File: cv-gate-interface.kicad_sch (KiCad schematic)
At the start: 19 parts, among them J3 Conn_01x06_Pin, J4 Conn_01x06_Pin, SW1 SW_SPST, U1 TL072

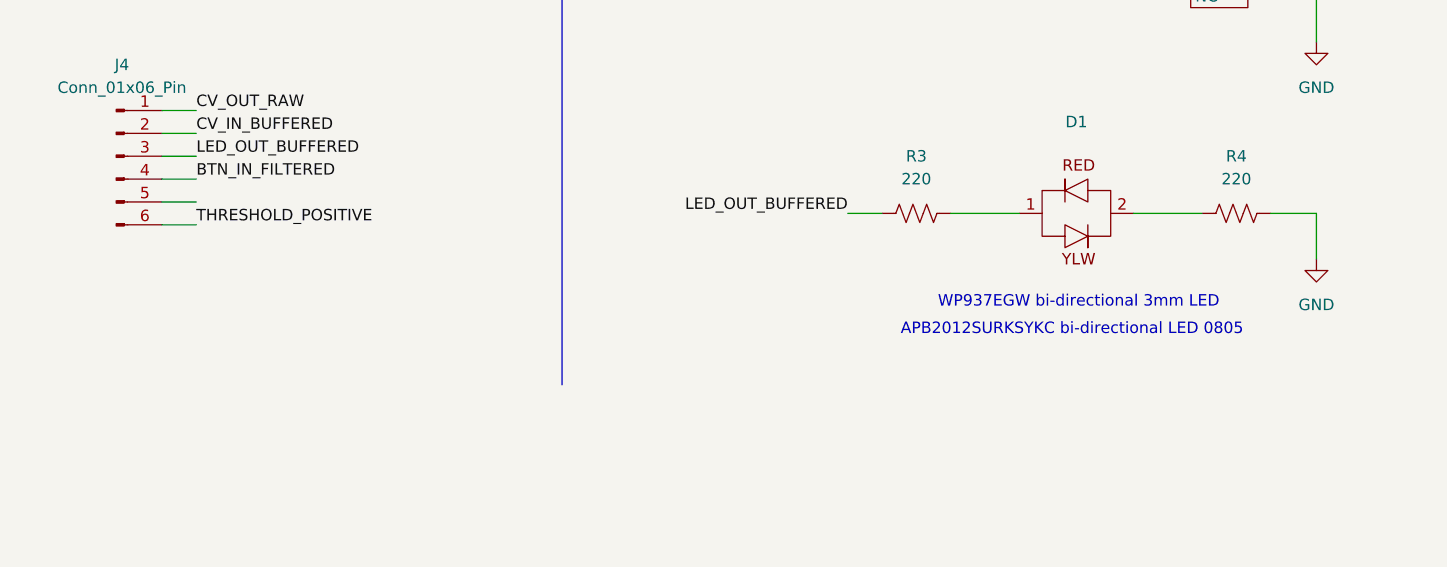
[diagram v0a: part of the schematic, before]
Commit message: Changed pot to 10K, fixed routing
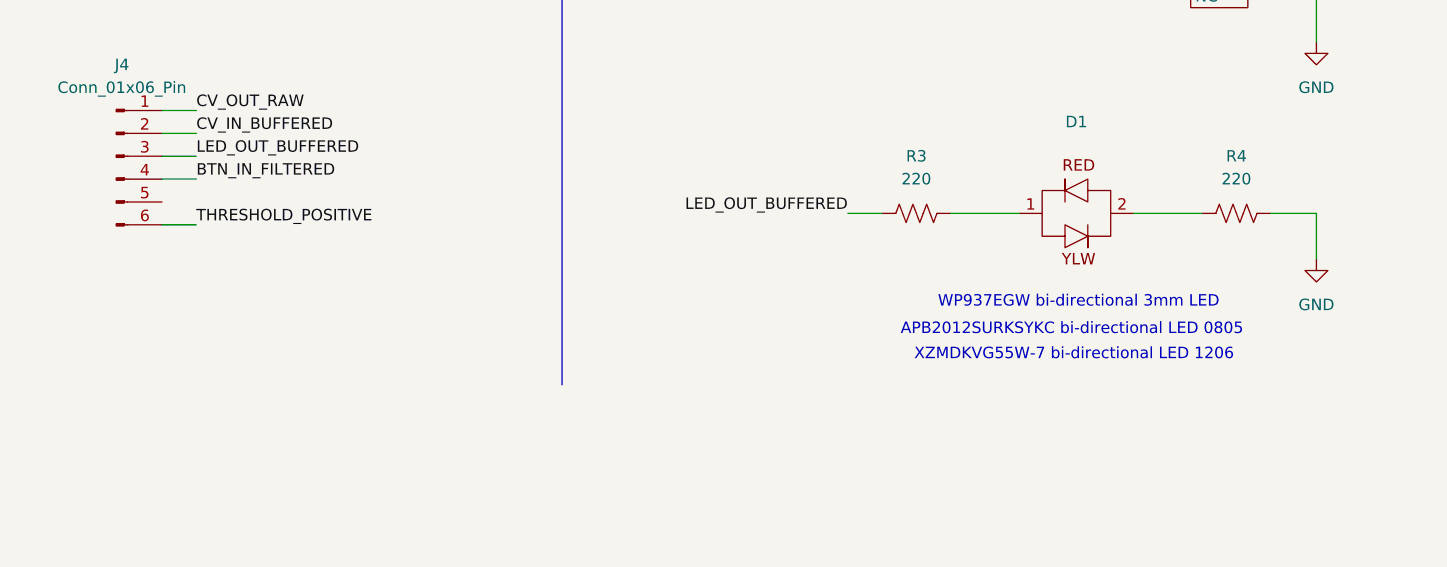
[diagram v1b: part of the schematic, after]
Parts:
- removed D1: ~, LED_THT:LED_D3.0mm, symbol mjrskiles:WP937EGW
- added D1: ~, mjrskiles:XZMDKVG55W-7, symbol mjrskiles:LED_BIPOLAR
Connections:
- net at R4.1: now also D1.2
- net at R3.2: now also D1.1
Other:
- note added: "XZMDKVG55W-7 bi-directional LED 1206"
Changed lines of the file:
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@@
+		)
+	)
+	(text "XZMDKVG55W-7 bi-directional LED 1206"
+		(exclude_from_sim no)
+		(at 234.696 160.528 0)
+		(effects
+			(font
+				(size 1.27 1.27)
+			)
 		)
 	)
@@
 		(pts
 			(xy 39.37 44.45) (xy 44.45 44.45)
-		)
-		(stroke
-			(width 0)
-			(type default)
-		)
-	)
-	(wire
-		(pts
-			(xy 133.35 143.51) (xy 137.16 143.51)
 		)
 		(stroke
@@
 	)
 	(symbol
+		(lib_id "mjrskiles:LED_BIPOLAR")
+		(at 233.68 144.78 0)
+		(unit 1)
+		(exclude_from_sim no)
+		(in_bom yes)
+		(on_board yes)
+		(dnp no)
+		(fields_autoplaced yes)
+		(property "Reference" "D1"
+			(at 234.95 134.62 0)
+			(effects
+				(font
+					(size 1.27 1.27)
+				)
+			)
+		)
+		(property "Value" "~"
+			(at 234.95 137.16 0)
+			(effects
+				(font
+					(size 1.27 1.27)
+				)
+			)
+		)
+		(property "Footprint" "mjrskiles:XZMDKVG55W-7"
+			(at 233.68 144.78 0)
+			(effects
+				(font
+					(size 1.27 1.27)
+				)
+				(hide yes)
+			)
+		)
+		(property "Datasheet" ""
+			(at 233.68 144.78 0)
+			(effects
+				(font
+					(size 1.27 1.27)
+				)
+				(hide yes)
+			)
+		)
+		(property "Description" "Bi-directional LED Red/Green 3mm"
+			(at 233.68 144.78 0)
+			(effects
+				(font
+					(size 1.27 1.27)
+				)
+				(hide yes)
+			)
+		)
+		(pin "1"
+		)
+		(pin "2"
+		)
+		(instances
+			(project ""
+				(path "/fbaa74aa-a0d2-45f6-b5af-948d50bbde7a"
+					(reference "D1")
+					(unit 1)
+				)
+			)
+		)
+	)
+	(symbol
 		(lib_id "Device:R_US")
 		(at 252.73 144.78 90)
@@
 				)
 			)
-		)
-	)
-	(symbol
-		(lib_id "mjrskiles:WP937EGW")
-		(at 233.68 144.78 0)
-		(unit 1)
-		(exclude_from_sim no)
-		(in_bom yes)
-		(on_board yes)
-		(dnp no)
-		(fields_autoplaced yes)
-		(property "Reference" "D1"
-			(at 234.95 134.62 0)
-			(effects
-				(font
-					(size 1.27 1.27)
-				)
-			)
-		)
-		(property "Value" "~"
-			(at 234.95 137.16 0)
-			(effects
-				(font
-					(size 1.27 1.27)
-				)
-			)
-		)
-		(property "Footprint" "LED_THT:LED_D3.0mm"
-			(at 233.68 144.78 0)
-			(effects
-				(font
-					(size 1.27 1.27)
-				)
-				(hide yes)
-			)
-		)
-		(property "Datasheet" ""
-			(at 233.68 144.78 0)
-			(effects
-				(font
-					(size 1.27 1.27)
-				)
-				(hide yes)
-			)
-		)
-		(property "Description" "Bi-directional LED Red/Green 3mm"
-			(at 233.68 144.78 0)
-			(effects
-				(font
-					(size 1.27 1.27)
-				)
-				(hide yes)
-			)
-		)
-		(pin "1"
-		)
-		(pin "2"
-		)
-		(instances
-			(project ""
-				(path "/fbaa74aa-a0d2-45f6-b5af-948d50bbde7a"
-					(reference "D1")
-					(unit 1)
-				)
-			)
